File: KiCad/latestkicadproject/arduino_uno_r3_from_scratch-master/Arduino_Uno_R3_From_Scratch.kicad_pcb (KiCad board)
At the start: 2 copper layers, 50.8 x 58.4 mm, 36 parts, among them IC1 MC33269ST-5.OT3, IC5 ATMEGA328P-MU, P1 CONN_01X06, P2 IOH, P3 AD, P4 H4, SW1 RESET_SWITCH, U2 LP2985-33DBVR, U3 74AHC1G04, U4 74AHC1G04, U9 L298, X1 DG3XX-04-3.5, X2 DG3XX-02-3.5, Y2 Crystal

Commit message: PCB routing v1
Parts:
- removed U2: LP2985-33DBVR, LP2985-33DBVR:SOT95P280X145-5N
- removed U9: L298, L298P:SOIC127P1420X360-21N
- added IC2: MC33269ST-5.OT3, MC33269ST-3.3T3G:SOT230P700X175-4N, B.Cu at (100.6, 105.8)
- added IC3: L298P, L298Poud:SOIC127P1420X360-21N, B.Cu at (82.7, 79.1)
- C7: footprint Capacitors_SMD:C_0805_HandSoldering -> Capacitors_SMD:CP_Elec_4x5.3; moved to B.Cu
- SW1: moved to B.Cu
- moved C7 17.4 mm to (62.5, 77.3), turned to 270 degrees
- moved SW1 4.71 mm to (72.1, 83.9)
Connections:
- ICSP2 pad 6: GND -> Net-(ICSP2-Pad6)
- SW1 pad 1: Net-(SW1-Pad1) -> GND
- SW1 pad 2: Net-(SW1-Pad1) -> GND
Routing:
- net /ATMEGA328P/DIRA: track 235.0 -> 135.5 mm
- net +5V: track 157.3 -> 181.8 mm
- net GND: track 239.0 -> 263.4 mm, vias 2 -> 4
- net /Driver/OUT2: track 45.8 -> 62.7 mm
- net /Driver/PWRIN: track 6.32 -> 23.1 mm, vias 1 -> 2
- net /Headers/+3V3: track 9.22 -> 20.1 mm
- net /ATMEGA328P/PWMB: track 85.9 -> 95.9 mm
- net /Driver/OUT1: track 47.7 -> 53.2 mm
- net Net-(SW1-Pad1): track 4.50 -> 0.00 mm
- net /ATMEGA328P/DIRB: track 74.9 -> 77.0 mm
- net /Driver/OUT4: track 34.6 -> 36.5 mm
- net /Driver/OUT3: track 26.1 -> 24.2 mm
- net /ATMEGA328P/PWMA: track 38.7 -> 37.4 mm
- net Net-(ICSP2-Pad6): track 0.00 -> 1.27 mm
- net /ATMEGA328P/IO7: track 8.09 -> 7.12 mm
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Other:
- net class 0.5: via_dia 0.6 -> 0.7; via_drill 0.4 -> 0.5
- net class 30mills added: clearance 0.25, trace_width 0.75, via_dia 0.7, via_drill 0.5
- net class 40mills: clearance 1.016 -> 0.25; trace_width 1.016 -> 1

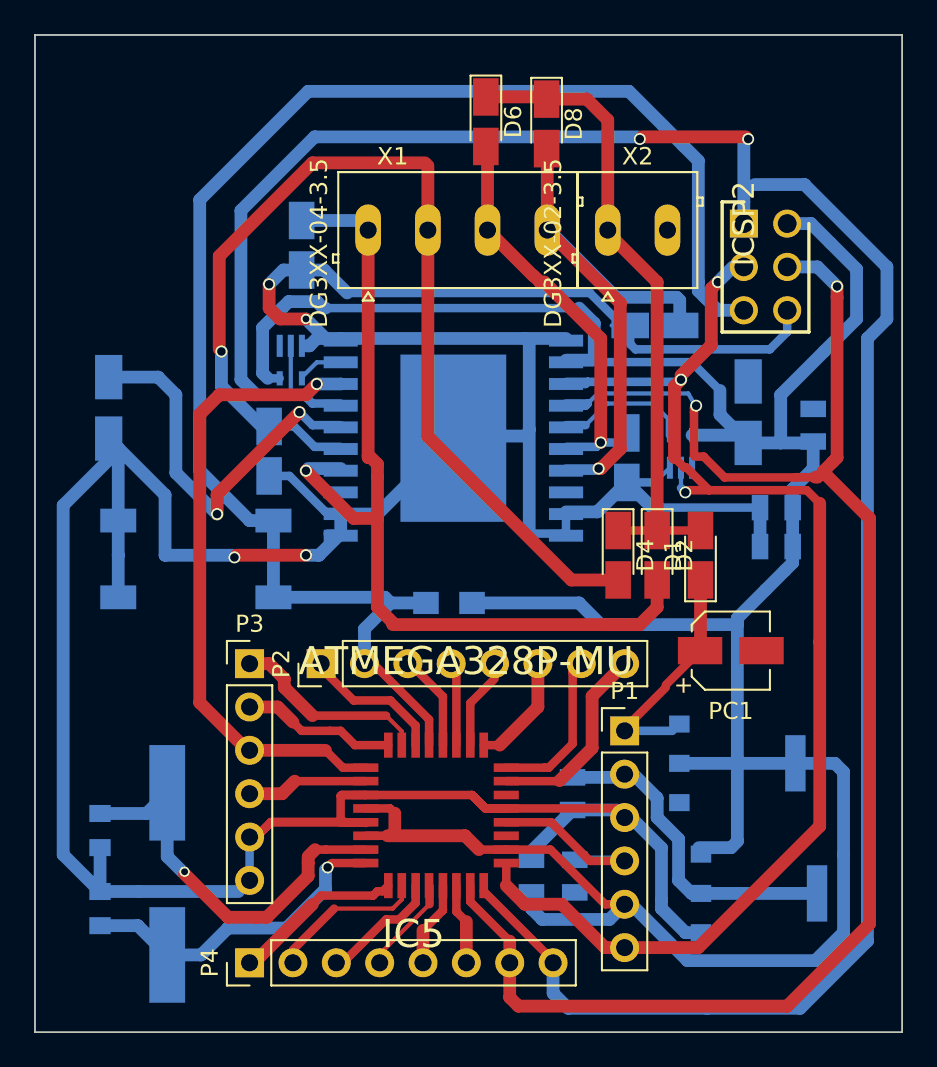
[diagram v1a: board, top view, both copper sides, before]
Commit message: correctie gnd-fouten
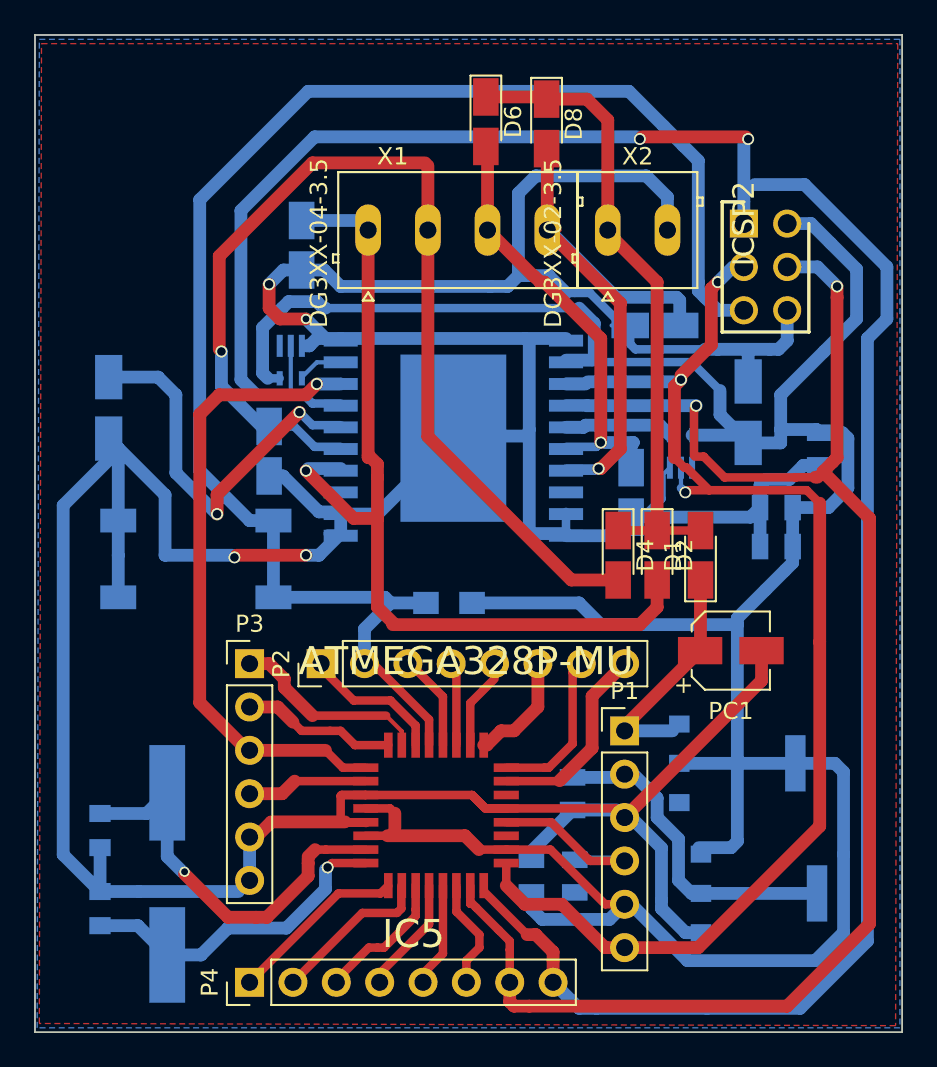
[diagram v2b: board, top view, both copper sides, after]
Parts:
- moved D7 2.05 mm to (93.1, 82.3)
- moved C2 1.45 mm to (104.1, 79.8), turned to 270 degrees
- moved P4 1.14 mm to (70.7, 111.0)
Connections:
- C2 pad 2: Net-(C2-Pad2) -> GND
- ICSP2 pad 6: Net-(ICSP2-Pad6) -> GND
- PC1 pad 2: Net-(PC1-Pad2) -> GND
- PC2 pad 2: Net-(PC2-Pad2) -> GND
- X2 pad 2: Net-(X2-Pad2) -> GND
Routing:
- net GND: track 263.4 -> 301.7 mm
- net +5V: track 181.8 -> 186.3 mm
- net /ATMEGA328P/SS: track 4.76 -> 6.54 mm
- net /Driver/OUT3: track 24.2 -> 25.9 mm
- net /ATMEGA328P/IO8: track 5.74 -> 7.04 mm
- net Net-(ICSP2-Pad6): track 1.27 -> 0.00 mm
- net /ATMEGA328P/IO9: track 5.01 -> 6.15 mm
- net /ATMEGA328P/IO7: track 7.12 -> 8.11 mm
- net /ATMEGA328P/IO6: track 9.17 -> 9.88 mm
- added copper zone on B.Cu, net (none)
- added copper zone on F.Cu, net (none)
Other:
- net class 12mills added: clearance 0.25, trace_width 0.3, via_dia 0.6, via_drill 0.4

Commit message: verbeteringen kicad
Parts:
- moved IC1 1.66 mm to (101.0, 98.3)
- moved C6 1.15 mm to (86.1, 104.9)
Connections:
- C4 pad 2: Net-(C4-Pad2) -> GND
- IC1 pad 1: Net-(IC1-Pad1) -> GND
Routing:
- net GND: track 301.7 -> 304.3 mm, vias 4 -> 5
- net +5V: track 186.3 -> 188.7 mm
- net /Headers/VIN: track 14.2 -> 16.3 mm
- net /Driver/PWRIN: track 23.1 -> 25.2 mm
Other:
- net class 15mills added: clearance 0.25, trace_width 0.38, via_dia 0.6, via_drill 0.4
- net class 30mills: via_dia 0.7 -> 1

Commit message: PCBtotaal
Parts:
- C1: value 1uF -> 0.11uF
- moved D5 13.6 mm to (62.2, 70.2)
- moved X1 9.46 mm to (75.7, 60.8)
- moved X2 6.35 mm to (93.5, 60.6)
- moved D1 3.81 mm to (100.6, 87.6), turned to 180 degrees
- moved C2 1.78 mm to (105.9, 79.9)
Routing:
- net /Motor Outputs/PWRIN: track 37.8 -> 77.9 mm
- net /Driver/OUT4: track 36.5 -> 69.8 mm
- net /Driver/OUT2: track 62.7 -> 84.8 mm, vias 1 -> 2
- net /ATMEGA328P/DIRA: track 135.4 -> 157.0 mm, vias 2 -> 3
- net /Driver/OUT3: track 25.9 -> 44.3 mm
- net /Driver/OUT1: track 53.2 -> 69.7 mm
- net /ATMEGA328P/RESET: track 90.2 -> 103.0 mm, vias 0 -> 1
- net GND: track 304.3 -> 314.9 mm, vias 5 -> 6
- net +5V: track 188.7 -> 199.3 mm, vias 0 -> 1
- net (no net): track 0.00 -> 4.70 mm
- net /Headers/VIN: track 16.3 -> 20.3 mm
- net /ATMEGA328P/DIRB: track 76.6 -> 80.1 mm, vias 3 -> 2
- net /Driver/PWRIN: track 25.2 -> 26.7 mm
- net /ATMEGA328P/PWMB: track 95.5 -> 94.3 mm, vias 2 -> 1
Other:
- board size 50.8 x 58.4 mm -> 53.1 x 73.2 mm
- net class 30mills: via_dia 1 -> 1.2
- board text added: "+"
